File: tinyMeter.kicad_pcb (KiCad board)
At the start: 2 copper layers, 74.6 x 70 mm, 93 parts, among them J1 USB_MASTER, J2 DC_POWER, J3 USB_POWER, J4 USBA_OUT_2, J5 USBA_OUT_1, J6 DC_POWER, J7 Debug, J8 External antenna, Q1 100N03A, Q2 100N03A, Q3 100N03A, Q4 SS8050, SW1 SW_Push, SW2 SW_Push, SW3 SW_Push, SW4 SW_Push, SW5 SW_Push, SW6 Boot, SW7 Reset, U1 ESP32-S3, U2 INA219AxD, U3 INA219AxD, U4 INA219AxD, U5 AMS1117-3.3, Y1 Crystal_GND24

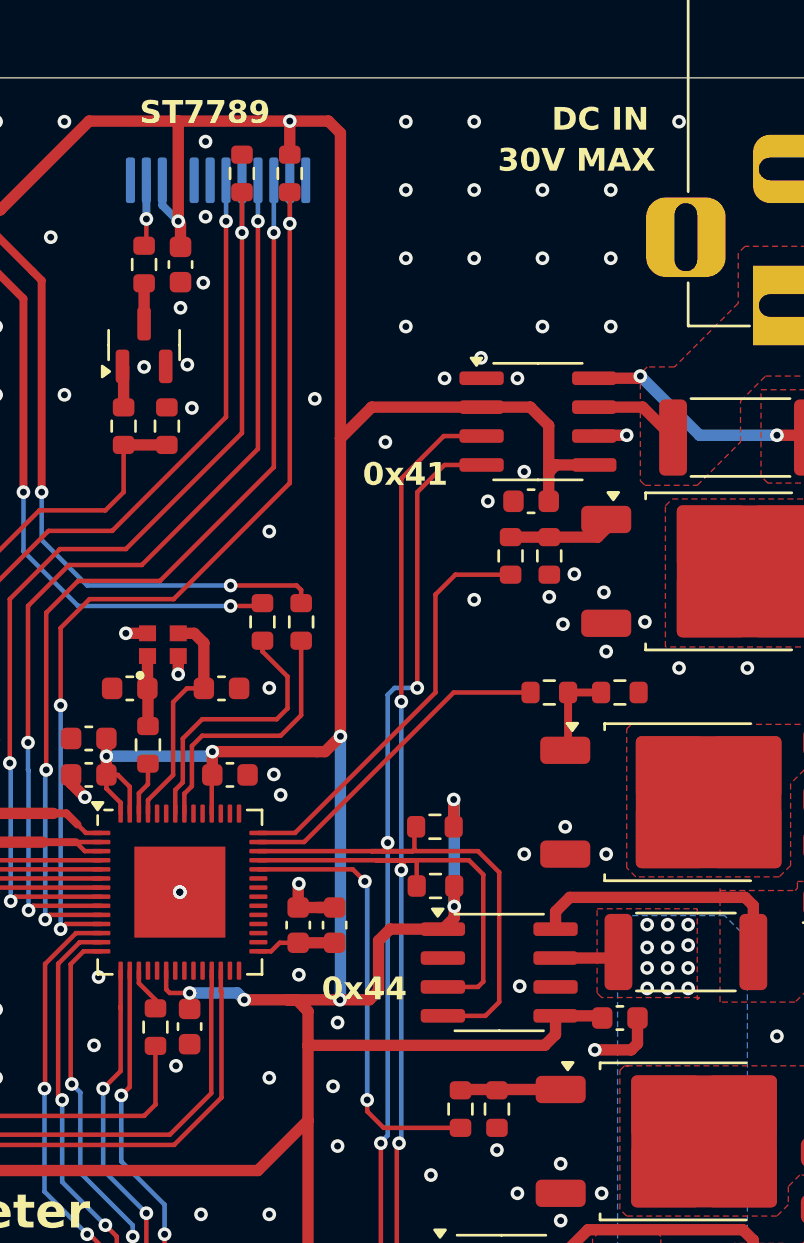
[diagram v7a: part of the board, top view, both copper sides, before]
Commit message: Fix DC voltage rating
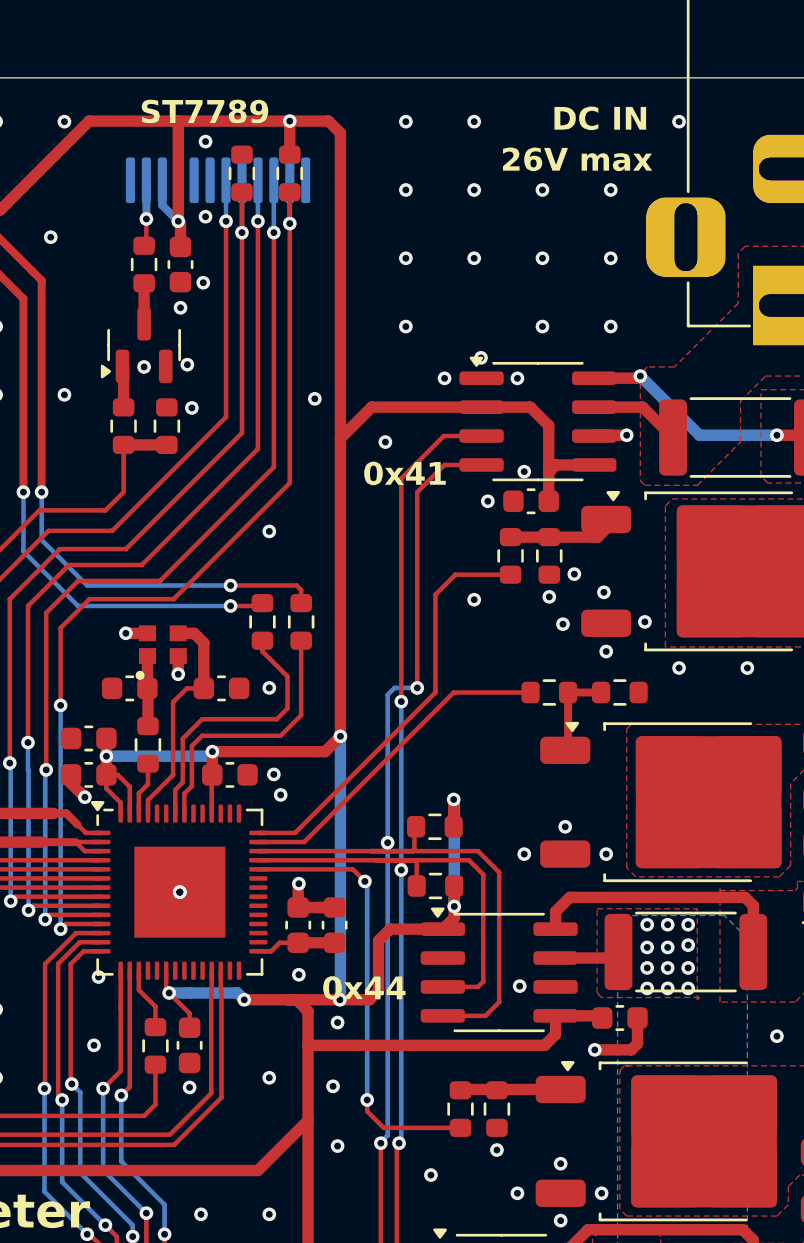
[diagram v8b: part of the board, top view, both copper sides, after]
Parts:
- moved C16 0.83 mm to (172.5, 116.9)
- moved R12 0.83 mm to (171.0, 116.9)
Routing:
- net +3V3: track 278.9 -> 280.1 mm
- net /MCU_LED_DIN: track 50.9 -> 50.1 mm
- net /MCU_LED_DATA: track 1.96 -> 2.78 mm
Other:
- board text added: "26V max"
- board text removed: "30V MAX"
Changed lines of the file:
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@@
 		(tags "resistor")
 		(property "Reference" "R27"
-			(at 0 -1.43 360)
+			(at 0 -1.43 0)
 			(layer "F.SilkS")
 			(hide yes)
@@
 		)
 		(property "Value" "2k7"
-			(at 0 1.43 360)
+			(at 0 1.43 0)
 			(layer "F.Fab")
 			(effects
@@
 		)
 		(fp_text user "${REFERENCE}"
-			(at 0 0 360)
+			(at 0 0 0)
 			(layer "F.Fab")
 			(effects
@@
 		(tags "resistor")
 		(property "Reference" "R22"
-			(at 0 -1.43 360)
+			(at 0 -1.43 0)
 			(layer "F.SilkS")
 			(hide yes)
@@
 		)
 		(property "Value" "10k"
-			(at 0 1.43 360)
+			(at 0 1.43 0)
 			(layer "F.Fab")
 			(effects
@@
 		)
 		(fp_text user "${REFERENCE}"
-			(at 0 0 360)
+			(at 0 0 0)
 			(layer "F.Fab")
 			(effects
@@
 	(footprint "Capacitor_SMD:C_0603_1608Metric"
 		(layer "F.Cu")
-		(at 172.5 116.075 -90)
+		(at 172.5 116.9 -90)
 		(descr "Capacitor SMD 0603 (1608 Metric), square (rectangular) end terminal, IPC_7351 nominal, (Body size source: IPC-SM-782 page 76, https://www.pcb-3d.com/wordpress/wp-content/uploads/ipc-sm-782a_amendment_1_and_2.pdf), generated with kicad-footprint-generator")
 		(tags "capacitor")
@@
 		(tags "resistor")
 		(property "Reference" "R21"
-			(at 0 -1.43 360)
+			(at 0 -1.43 0)
 			(layer "F.SilkS")
 			(hide yes)
@@
 		)
 		(property "Value" "1k"
-			(at 0 1.43 360)
+			(at 0 1.43 0)
 			(layer "F.Fab")
 			(effects
@@
 		)
 		(fp_text user "${REFERENCE}"
-			(at 0 0 360)
+			(at 0 0 0)
 			(layer "F.Fab")
 			(effects
@@
 		(tags "resistor")
 		(property "Reference" "R26"
-			(at 0 -1.43 360)
+			(at 0 -1.43 0)
 			(layer "F.SilkS")
 			(hide yes)
@@
 		)
 		(property "Value" "2k7"
-			(at 0 1.43 360)
+			(at 0 1.43 0)
 			(layer "F.Fab")
 			(effects
@@
 		)
 		(fp_text user "${REFERENCE}"
-			(at 0 0 360)
+			(at 0 0 0)
 			(layer "F.Fab")
 			(effects
@@
 		(tags "resistor")
 		(property "Reference" "R13"
-			(at 0 -1.43 360)
+			(at 0 -1.43 0)
 			(layer "F.SilkS")
 			(hide yes)
@@
 		)
 		(property "Value" "220"
-			(at 0 1.43 360)
+			(at 0 1.43 0)
 			(layer "F.Fab")
 			(effects
@@
 		)
 		(fp_text user "${REFERENCE}"
-			(at 0 0 360)
+			(at 0 0 0)
 			(layer "F.Fab")
 			(effects
@@
 	(footprint "Resistor_SMD:R_0603_1608Metric"
 		(layer "F.Cu")
-		(at 171 116.1 90)
+		(at 171 116.925 90)
 		(descr "Resistor SMD 0603 (1608 Metric), square (rectangular) end terminal, IPC_7351 nominal, (Body size source: IPC-SM-782 page 72, https://www.pcb-3d.com/wordpress/wp-content/uploads/ipc-sm-782a_amendment_1_and_2.pdf), generated with kicad-footprint-generator")
 		(tags "resistor")
@@
 		)
 	)
-	(gr_text "30V MAX"
+	(gr_text "26V max"
 		(at 189.5 78.6 0)
 		(layer "F.SilkS" knockout)
@@
 	)
 	(via
+		(at 172.5 118.75)
+		(size 0.6)
+		(drill 0.3)
+		(layers "F.Cu" "B.Cu")
+		(free yes)
+		(net 1)
+	)
+	(via
 		(at 185 79.325)
 		(size 0.6)
@@
 	)
 	(via
-		(at 171.9 117.8)
-		(size 0.6)
-		(drill 0.3)
-		(layers "F.Cu" "B.Cu")
-		(free yes)
-		(net 1)
-	)
-	(via
 		(at 158 142.325)
 		(size 0.6)
@@
 	)
 	(segment
-		(start 172.5 115.3)
-		(end 172.5 114.6)
-		(width 0.2)
-		(layer "F.Cu")
-		(net 3)
-	)
-	(segment
 		(start 176.8 114.9)
 		(end 177.2 114.9)
@@
 	)
 	(segment
-		(start 171.625 114.6)
-		(end 172.5 114.6)
-		(width 0.2)
-		(layer "F.Cu")
-		(net 3)
-	)
-	(segment
 		(start 188.1 116.9)
 		(end 177.7 116.9)
@@
 	)
 	(segment
+		(start 171.47 114.47)
+		(end 172.5 115.5)
+		(width 0.2)
+		(layer "F.Cu")
+		(net 3)
+	)
+	(segment
 		(start 172 80.7)
 		(end 172 76.3)
@@
 	)
 	(segment
-		(start 171.625 114.6)
-		(end 171.47 114.445)
+		(start 172.5 115.5)
+		(end 172.5 116.125)
 		(width 0.2)
 		(layer "F.Cu")
@@
 	)
 	(segment
+		(start 171.47 113.62)
+		(end 171.47 114.47)
+		(width 0.2)
+		(layer "F.Cu")
+		(net 3)
+	)
+	(segment
 		(start 161.8 122.4)
 		(end 175.5 122.4)
@@
 	)
 	(segment
-		(start 171.47 114.445)
-		(end 171.47 113.62)
-		(width 0.2)
-		(layer "F.Cu")
-		(net 3)
-	)
-	(segment
 		(start 164.185661 80.2)
 		(end 168.085661 76.3)
@@
 	)
 	(via
-		(at 172.5 114.6)
+		(at 171.2 133.7)
 		(size 0.6)
 		(drill 0.3)
@@
 	)
 	(via
-		(at 171.2 133.7)
+		(at 171.6 114.6)
 		(size 0.6)
 		(drill 0.3)
@@
 	)
 	(segment
+		(start 172.5 114.6)
+		(end 171.6 114.6)
+		(width 0.5)
+		(layer "B.Cu")
+		(net 3)
+	)
+	(segment
 		(start 148.5 108.7)
 		(end 148.5 117.85)
@@
 	)
 	(segment
-		(start 171 114.9)
-		(end 170.27 114.17)
+		(start 170.27 114.47)
+		(end 171 115.2)
 		(width 0.2)
 		(layer "F.Cu")
@@
 	)
 	(segment
-		(start 171 115.275)
-		(end 171 114.9)
+		(start 171 115.2)
+		(end 171 116.1)
 		(width 0.2)
 		(layer "F.Cu")
@@
 	)
 	(segment
-		(start 170.27 114.17)
-		(end 170.27 113.62)
+		(start 170.27 113.62)
+		(end 170.27 114.47)
 		(width 0.2)
 		(layer "F.Cu")
@@
 	)
 	(segment
+		(start 171 117.75)
+		(end 171 119.5)
+		(width 0.2)
+		(layer "F.Cu")
+		(net 94)
+	)
+	(segment
 		(start 142.2 119)
 		(end 140.6 119)
@@
 		(width 0.2)
 		(layer "F.Cu")
-		(net 94)
-	)
-	(segment
-		(start 171 119.5)
-		(end 171 116.925)
-		(width 0.2)
-		(layer "F.Cu")
